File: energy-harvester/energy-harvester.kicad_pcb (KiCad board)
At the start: 2 copper layers, 46.2 x 15.7 mm, 16 parts, among them P1 CONN_2, P2 CONN_2, P3 CONN_2, P4 CONN_6, P5 CONN_6, U1 LTC3588-1

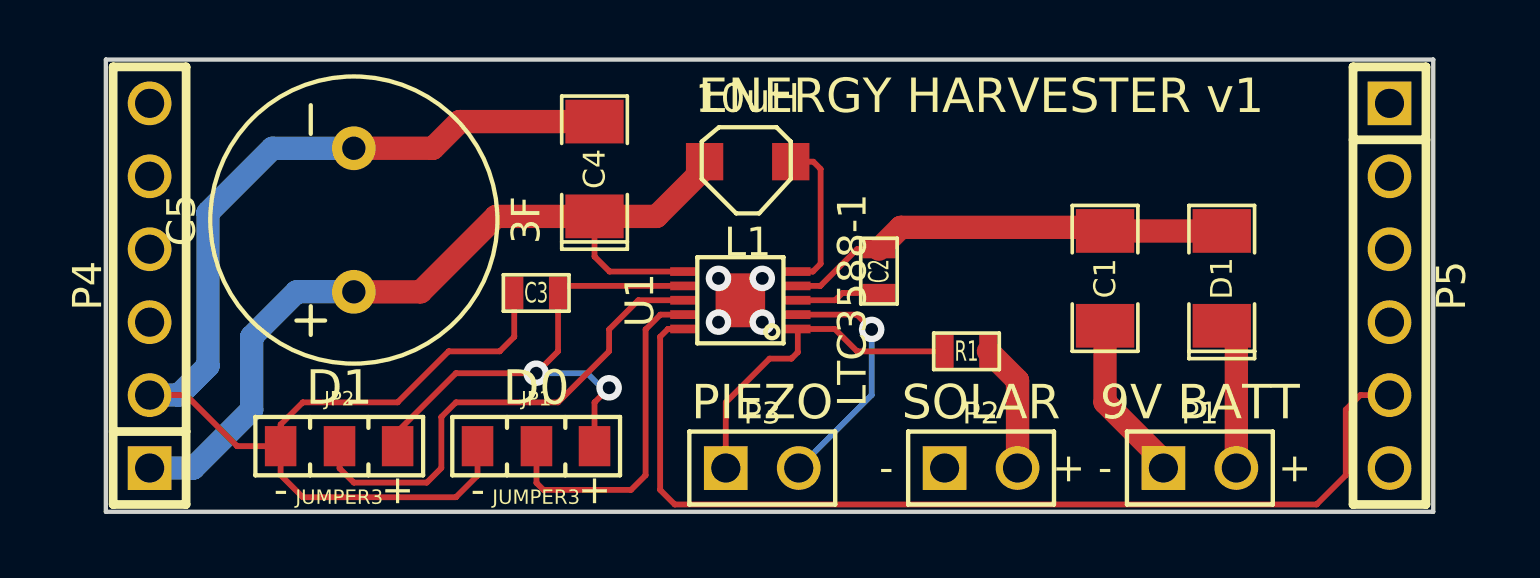
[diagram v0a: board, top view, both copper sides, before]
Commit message: energy-harverster: Add second super cap.
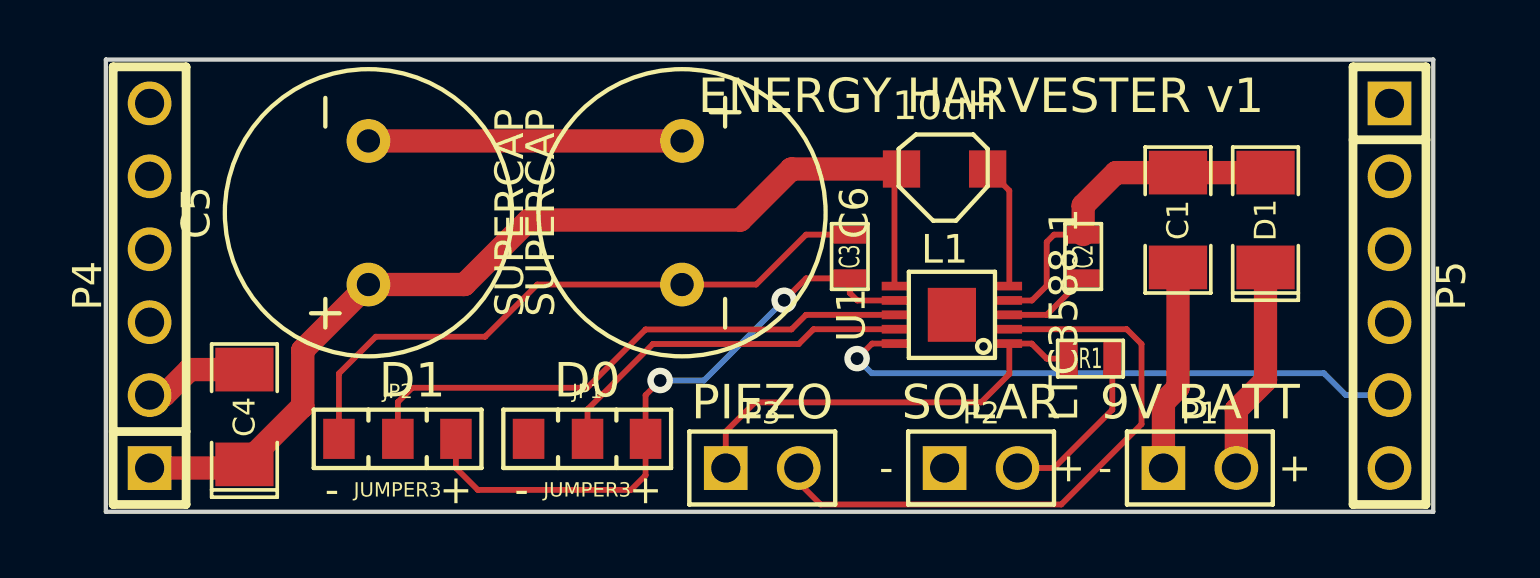
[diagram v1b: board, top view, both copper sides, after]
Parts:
- added C6: SUPERCAP, SUPERCAP_ESHSR-0010C0-002R7, F.Cu at (45.5, 44.5)
- C5: value 3F -> SUPERCAP
- moved C4 14.9 mm to (30.2, 51.6)
- moved C3 11.0 mm to (51.3, 46.0), turned to 90 degrees
- moved U1 7.38 mm to (54.9, 48.0)
- moved C2 7.13 mm to (59.4, 46.0)
- moved L1 6.86 mm to (54.6, 42.9)
- moved R1 4.33 mm to (59.7, 49.5)
- moved C1 3.25 mm to (62.7, 44.7)
- moved D1 2.54 mm to (65.8, 44.7)
- moved JP2 2.05 mm to (35.6, 52.3)
- moved JP1 1.80 mm to (42.2, 52.3)
- moved C5 0.57 mm to (34.5, 44.5)
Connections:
- C4 pad 1: N-0000022 (its old number) -> VCC
- C5 pad 1: N-0000022 (its old number) -> VCC
- C5 pad 2: GND -> N-0000014
- L1 pad 2: N-0000022 (its old number) -> VCC
- P4 pad 1: N-0000022 (its old number) -> VCC
- U1 pad 6: N-0000022 (its old number) -> VCC
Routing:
- net VCC: track 0.00 -> 35.8 mm
- net N-0000022 (its old number): track 30.1 -> 0.00 mm
- net GND: track 62.0 -> 32.9 mm, vias 4 -> 0
- net /PGOOD: track 34.8 -> 20.6 mm, vias 0 -> 1
- net N-0000012: track 8.66 -> 21.5 mm, vias 1 -> 0
- net N-0000014: track 0.00 -> 10.9 mm
- net N-0000011: track 11.8 -> 15.3 mm
- net N-0000023: track 15.7 -> 12.3 mm
- net /VIN2: track 18.7 -> 21.9 mm
- net N-0000013: track 17.1 -> 19.8 mm
- net N-0000017: track 5.16 -> 7.41 mm
- net N-0000020: track 4.48 -> 5.92 mm
- net N-0000022: track 5.35 -> 4.39 mm
- net N-0000015: track 12.0 -> 12.9 mm

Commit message: energy-harvester: Change some components, add logo.
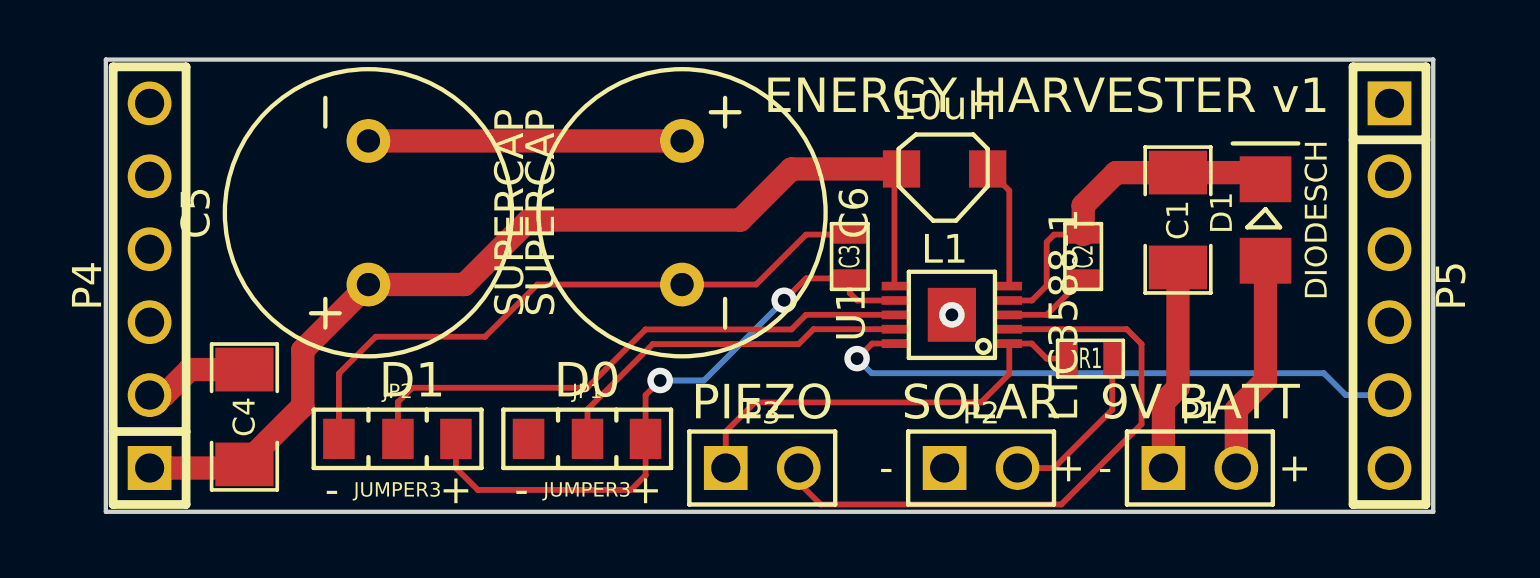
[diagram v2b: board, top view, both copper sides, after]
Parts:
- added ?: , LOGO_SNOWCAP_BACK, B.Cu at (59.4, 44.5)
- C4: footprint SM1206POL -> SM1206
- D1: footprint SM1206POL -> DIODE-1206
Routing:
- net GND: vias 0 -> 1
